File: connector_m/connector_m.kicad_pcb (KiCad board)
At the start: 2 copper layers, 85 x 47 mm, 33 parts, among them J1 PowerOut, J2 PowerIn, J3 CANFD_In, U1 SKA2P1_TX, U2 TJA1042T, U3 SKA2P1_RX, U5 XC6206P182MR, U6 LSF0102DCUR

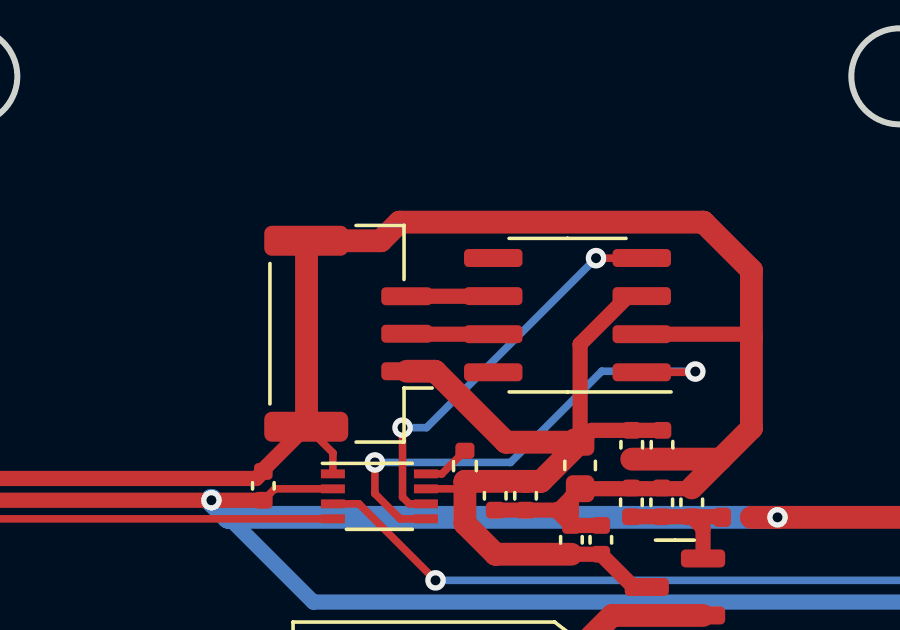
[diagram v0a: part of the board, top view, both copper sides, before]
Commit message: [Modify] Change CAN ports sequence
2pin: 1-CAN_L, 2-CAN_H
3pin: 1-5V, 2-CAN_L, 3-CAN_H
4pin: 1,2-CAN_L, 3,4-CAN_H

Signed-off-by: Homalozoa <nx.tardis@gmail.com>
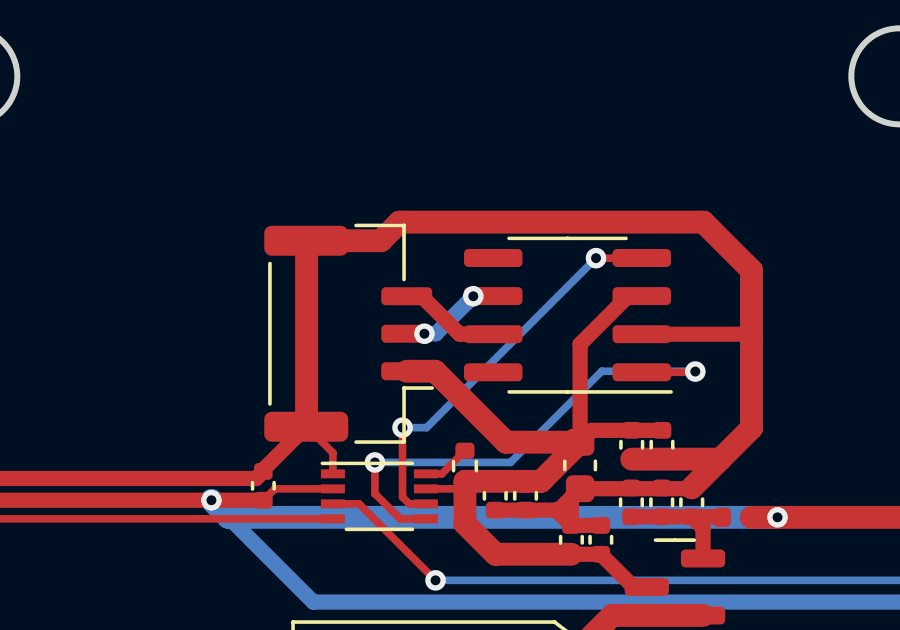
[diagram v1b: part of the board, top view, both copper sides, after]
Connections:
- J3 pad 2: CANFD_H -> CANFD_L
- J3 pad 3: CANFD_L -> CANFD_H
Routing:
- net CANFD_L: track 2.89 -> 3.43 mm, vias 0 -> 2
- net CANFD_H: track 2.89 -> 3.41 mm

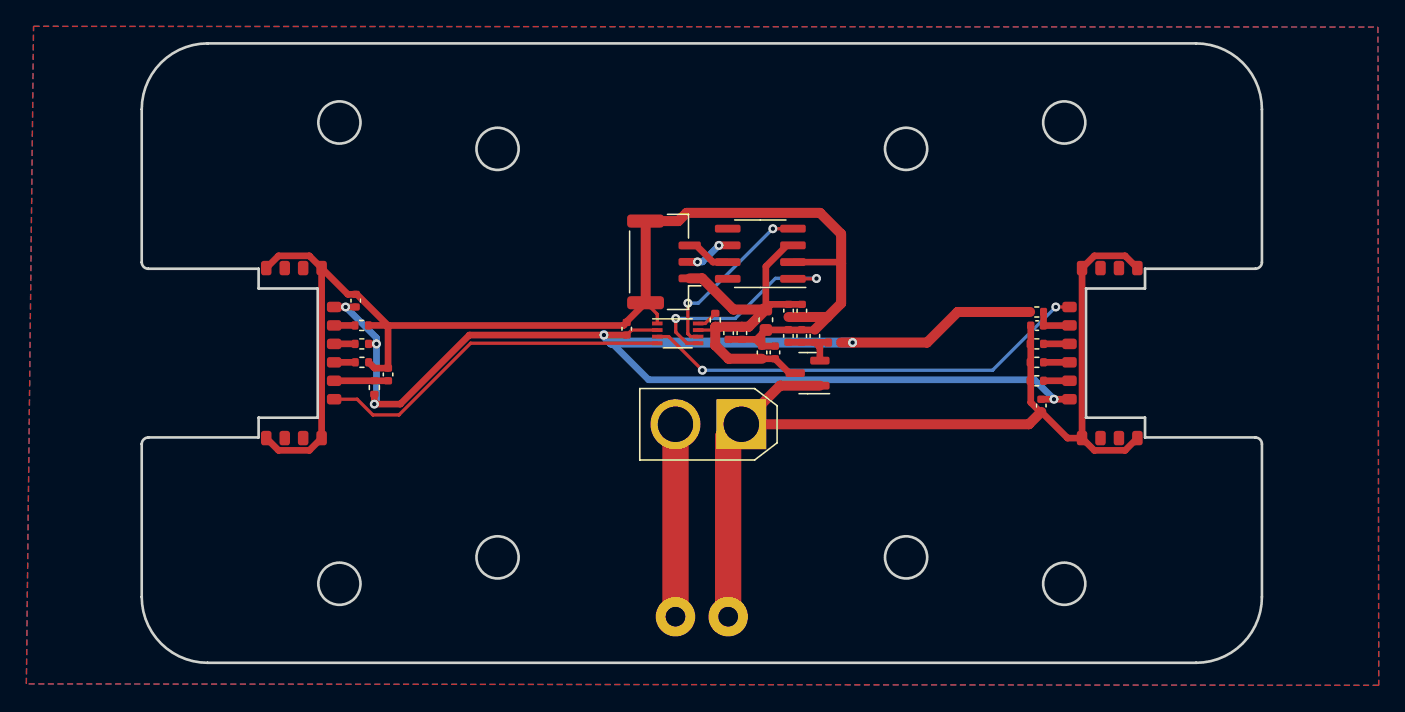
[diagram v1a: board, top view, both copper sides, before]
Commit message: [Fix] Manufacture modification
Signed-off-by: Homalozoa <nx.tardis@gmail.com>
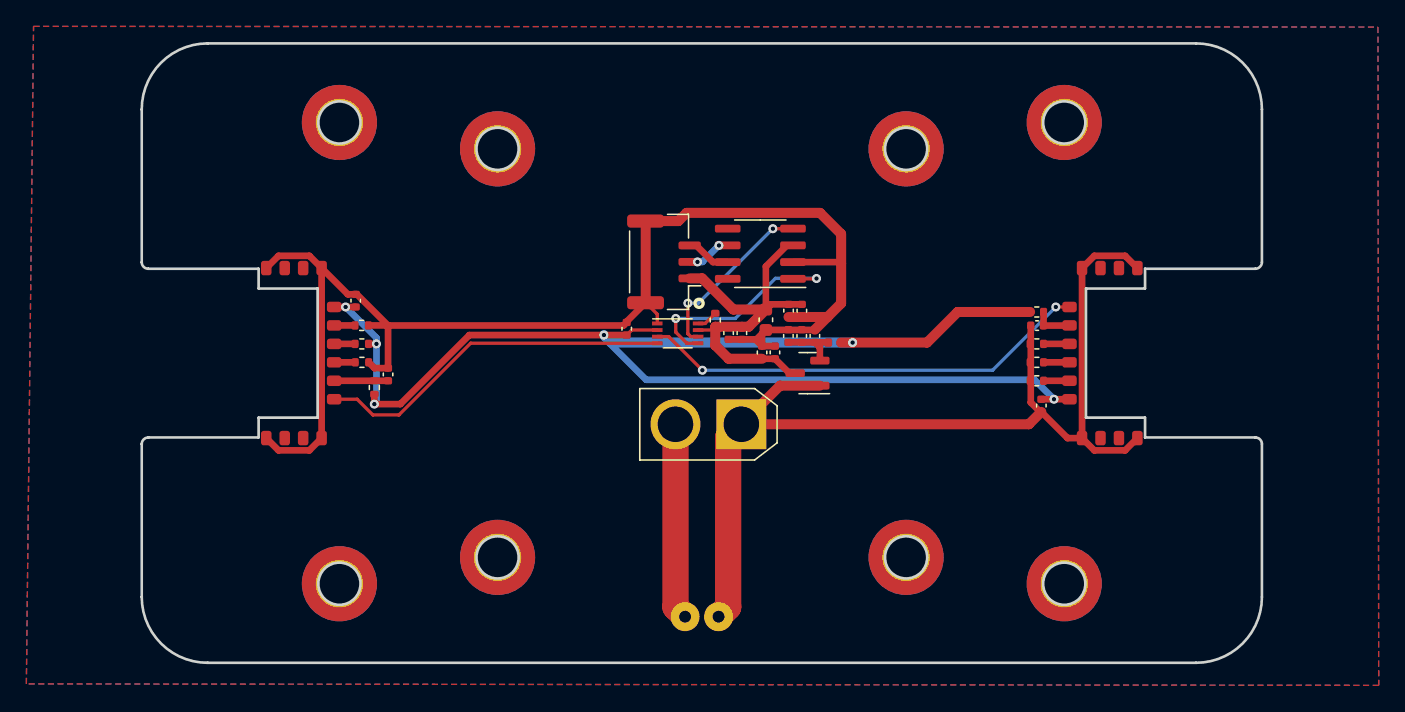
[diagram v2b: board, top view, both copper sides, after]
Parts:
- added REF**: MountingHole_3.2mm_M3_ISO7380_Pad_TopBottom, MountingHole:MountingHole_3.2mm_M3_ISO7380_Pad_TopBottom, F.Cu at (72.5, 42.5)
- added REF**: MountingHole_3.2mm_M3_ISO7380_Pad_TopBottom, MountingHole:MountingHole_3.2mm_M3_ISO7380_Pad_TopBottom, F.Cu at (72.5, 77.5)
- added REF**: MountingHole_3.2mm_M3_ISO7380_Pad_TopBottom, MountingHole:MountingHole_3.2mm_M3_ISO7380_Pad_TopBottom, F.Cu at (84.5, 44.5)
- added REF**: MountingHole_3.2mm_M3_ISO7380_Pad_TopBottom, MountingHole:MountingHole_3.2mm_M3_ISO7380_Pad_TopBottom, F.Cu at (127.5, 42.5)
- added REF**: MountingHole_3.2mm_M3_ISO7380_Pad_TopBottom, MountingHole:MountingHole_3.2mm_M3_ISO7380_Pad_TopBottom, F.Cu at (115.5, 75.5)
- added REF**: MountingHole_3.2mm_M3_ISO7380_Pad_TopBottom, MountingHole:MountingHole_3.2mm_M3_ISO7380_Pad_TopBottom, F.Cu at (84.5, 75.5)
- added REF**: MountingHole_3.2mm_M3_ISO7380_Pad_TopBottom, MountingHole:MountingHole_3.2mm_M3_ISO7380_Pad_TopBottom, F.Cu at (115.5, 44.5)
- added REF**: MountingHole_3.2mm_M3_ISO7380_Pad_TopBottom, MountingHole:MountingHole_3.2mm_M3_ISO7380_Pad_TopBottom, F.Cu at (127.5, 77.5)
- L2: value LQW15AN1N3D10D -> MLG1005S1N3BT000
